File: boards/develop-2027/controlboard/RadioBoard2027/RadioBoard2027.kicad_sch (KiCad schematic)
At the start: 0 parts

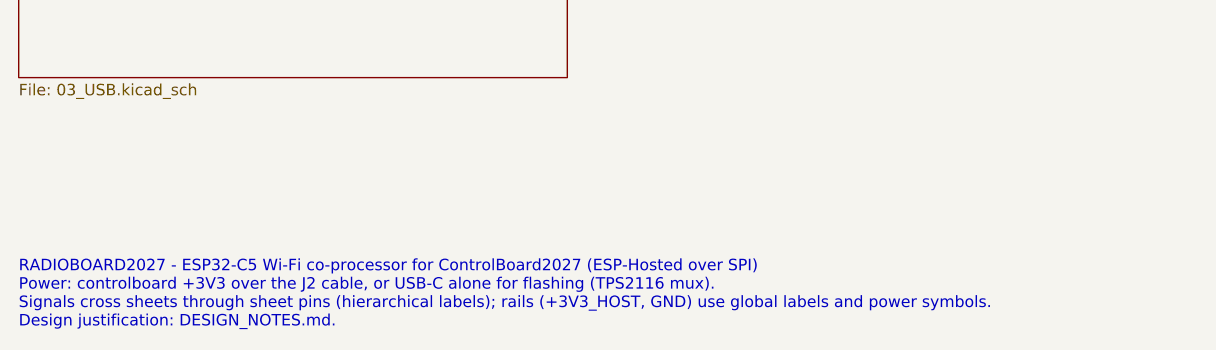
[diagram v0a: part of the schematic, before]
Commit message: Radio link: Samtec LSHM mezzanine on both boards
ControlBoard2027 J9 and RadioBoard2027 J2 move from the JST GH cable header
to the same hermaphroditic Samtec LSHM-110-02.5 (5mm stack); the radio sits
right side up, overhanging the controlboard's east edge on J2 alone.

- Pinout and physical mating checked by script over both boards (rigid
  placement, all 20 pads land on partner pads with matching nets).
- ControlBoard: radio SPI re-routed with 45-degree trapezoid length bumps,
  CS crossing in a 4.4mm B.Cu hop over an In2 GND patch (priority above the
  +3V3 plane), pull resistors on their lines, straight J9 power/GND buses,
  R32 10k (100k read high against the C5 GPIO4 reset pull-up).
- RadioBoard: J2 on B.Cu near the board centre, U5/U6 flow-through on F.Cu
  above it, D4 on B.Cu inline on +3V3_HOST, SPI re-matched end to end
  (SCK/MOSI/CS within 0.17mm), inner-layer via clearance rule closes the
  antipad slot under the row-gap vias.
- BOMs, DESIGN_NOTES, TODOs, sources, sheet notes and schematic PDF updated.
  DRC 0 errors / 0 unconnected / parity clean on both; ERC clean apart from
  the documented ControlBoard VCAP exception.

Co-Authored-By: Claude Opus 5.5 <noreply@anthropic.com>
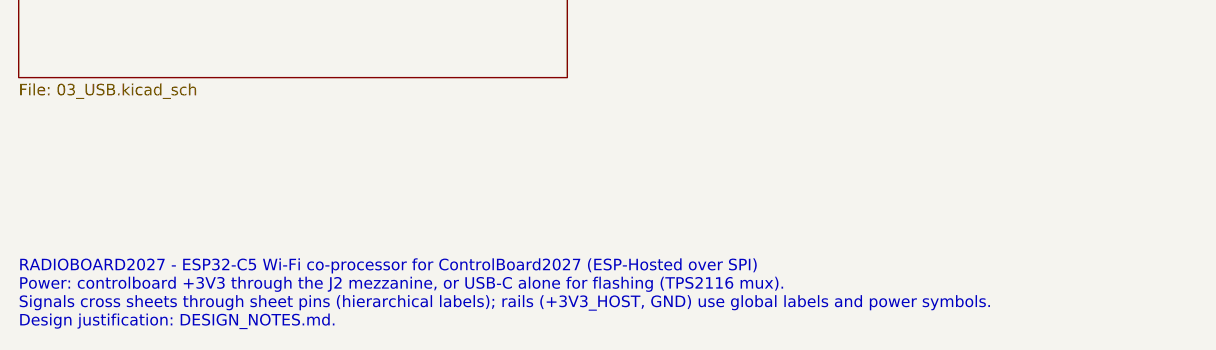
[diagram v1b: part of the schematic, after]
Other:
- note added: "RADIOBOARD2027 - ESP32-C5 Wi-Fi co-processor for ControlBoard2027 (ESP-Hosted over SPI) Power: controlboard +3V3 through the J2 mezzanine, or USB-C alone for flashing (TPS2116 mux). Signals cross sheets through sheet pins (hierarchical labels); rails (+3V3_HOST, GND) use global labels and power symbols. Design justification: DESIGN_NOTES.md."
- note removed: "RADIOBOARD2027 - ESP32-C5 Wi-Fi co-processor for ControlBoard2027 (ESP-Hosted over SPI) Power: controlboard +3V3 over the J2 cable, or USB-C alone for flashing (TPS2116 mux). Signals cross sheets through sheet pins (hierarchical labels); rails (+3V3_HOST, GND) use global labels and power symbols. Design justification: DESIGN_NOTES.md."
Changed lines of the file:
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@@
 		)
 	)
-	(text "RADIOBOARD2027 - ESP32-C5 Wi-Fi co-processor for ControlBoard2027 (ESP-Hosted over SPI)\nPower: controlboard +3V3 over the J2 cable, or USB-C alone for flashing (TPS2116 mux).\nSignals cross sheets through sheet pins (hierarchical labels); rails (+3V3_HOST, GND) use global labels and power symbols.\nDesign justification: DESIGN_NOTES.md."
+	(text "RADIOBOARD2027 - ESP32-C5 Wi-Fi co-processor for ControlBoard2027 (ESP-Hosted over SPI)\nPower: controlboard +3V3 through the J2 mezzanine, or USB-C alone for flashing (TPS2116 mux).\nSignals cross sheets through sheet pins (hierarchical labels); rails (+3V3_HOST, GND) use global labels and power symbols.\nDesign justification: DESIGN_NOTES.md."
 		(at 30.48 160.02 0)
 		(effects
